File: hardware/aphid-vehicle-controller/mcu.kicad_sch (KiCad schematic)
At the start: 19 parts, among them J3 MAIN_DEBUG, J4 SWD, U1 STM32G491CETx, Y1 8 MHz

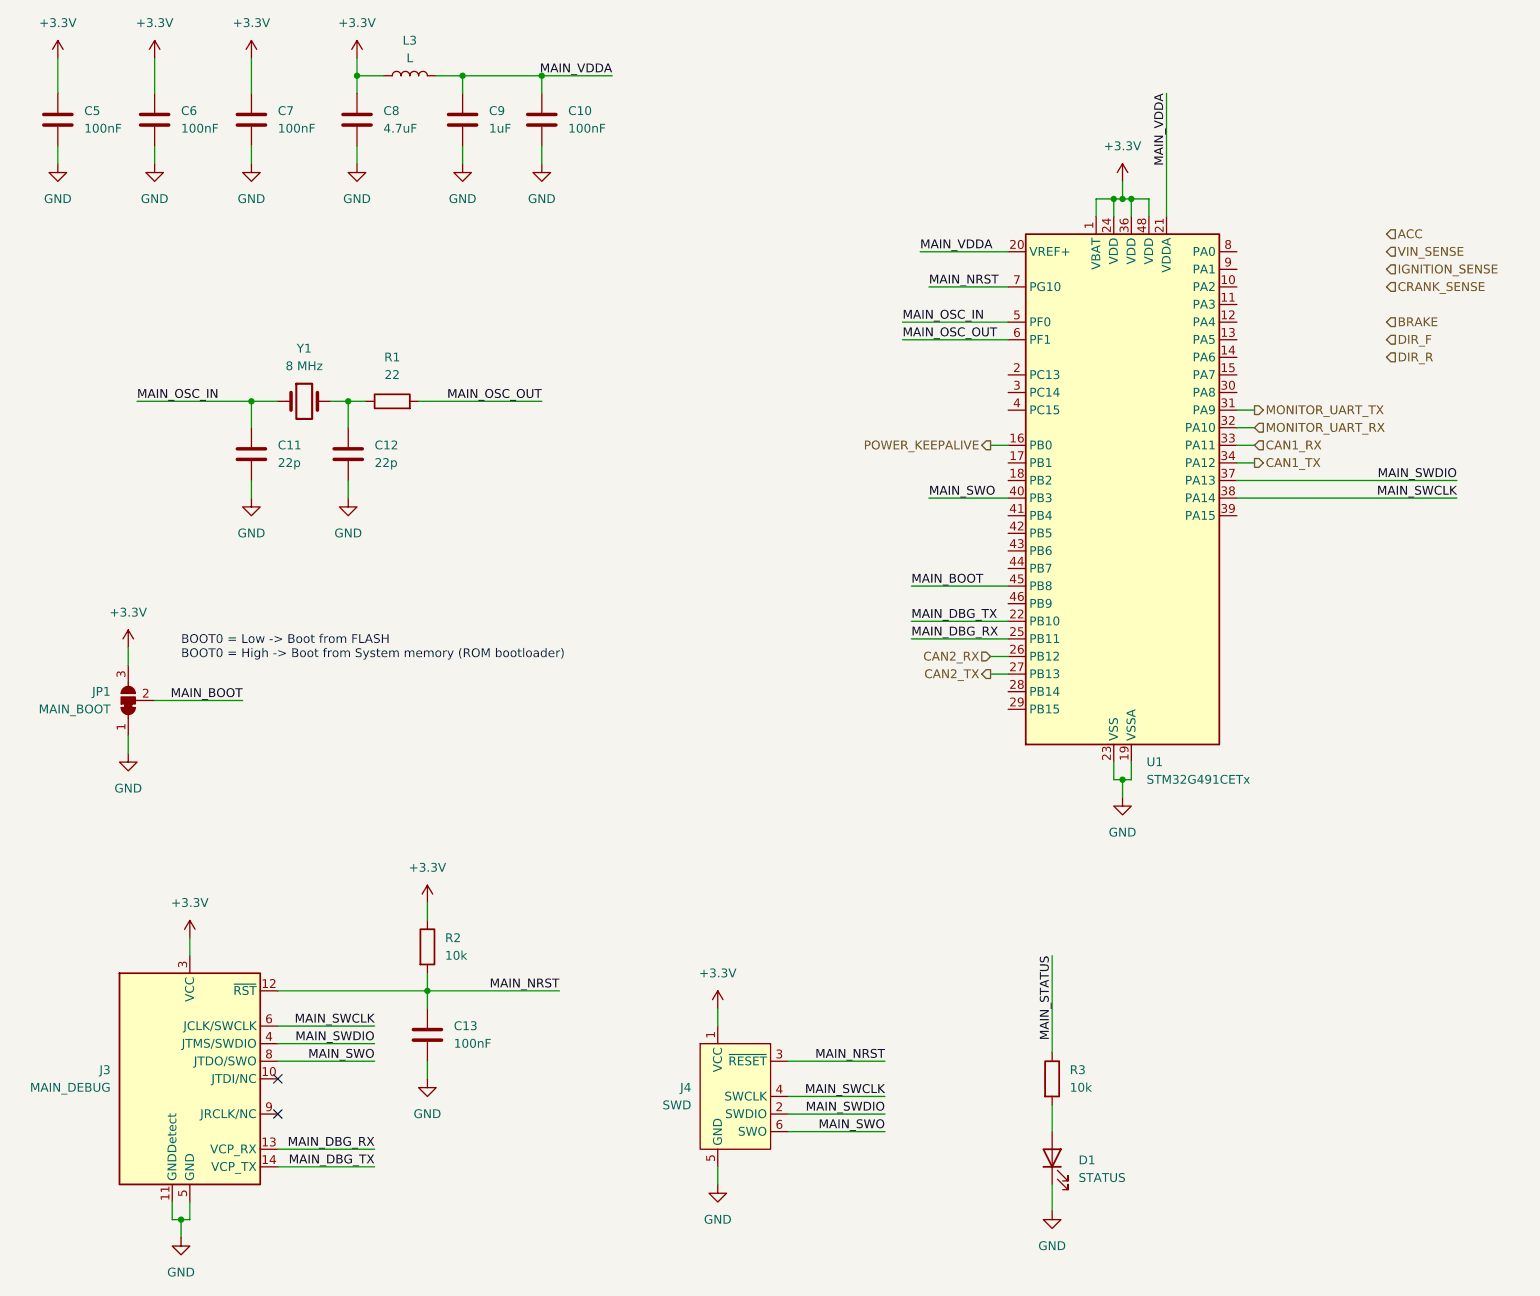
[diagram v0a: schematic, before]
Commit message: ERC check passing
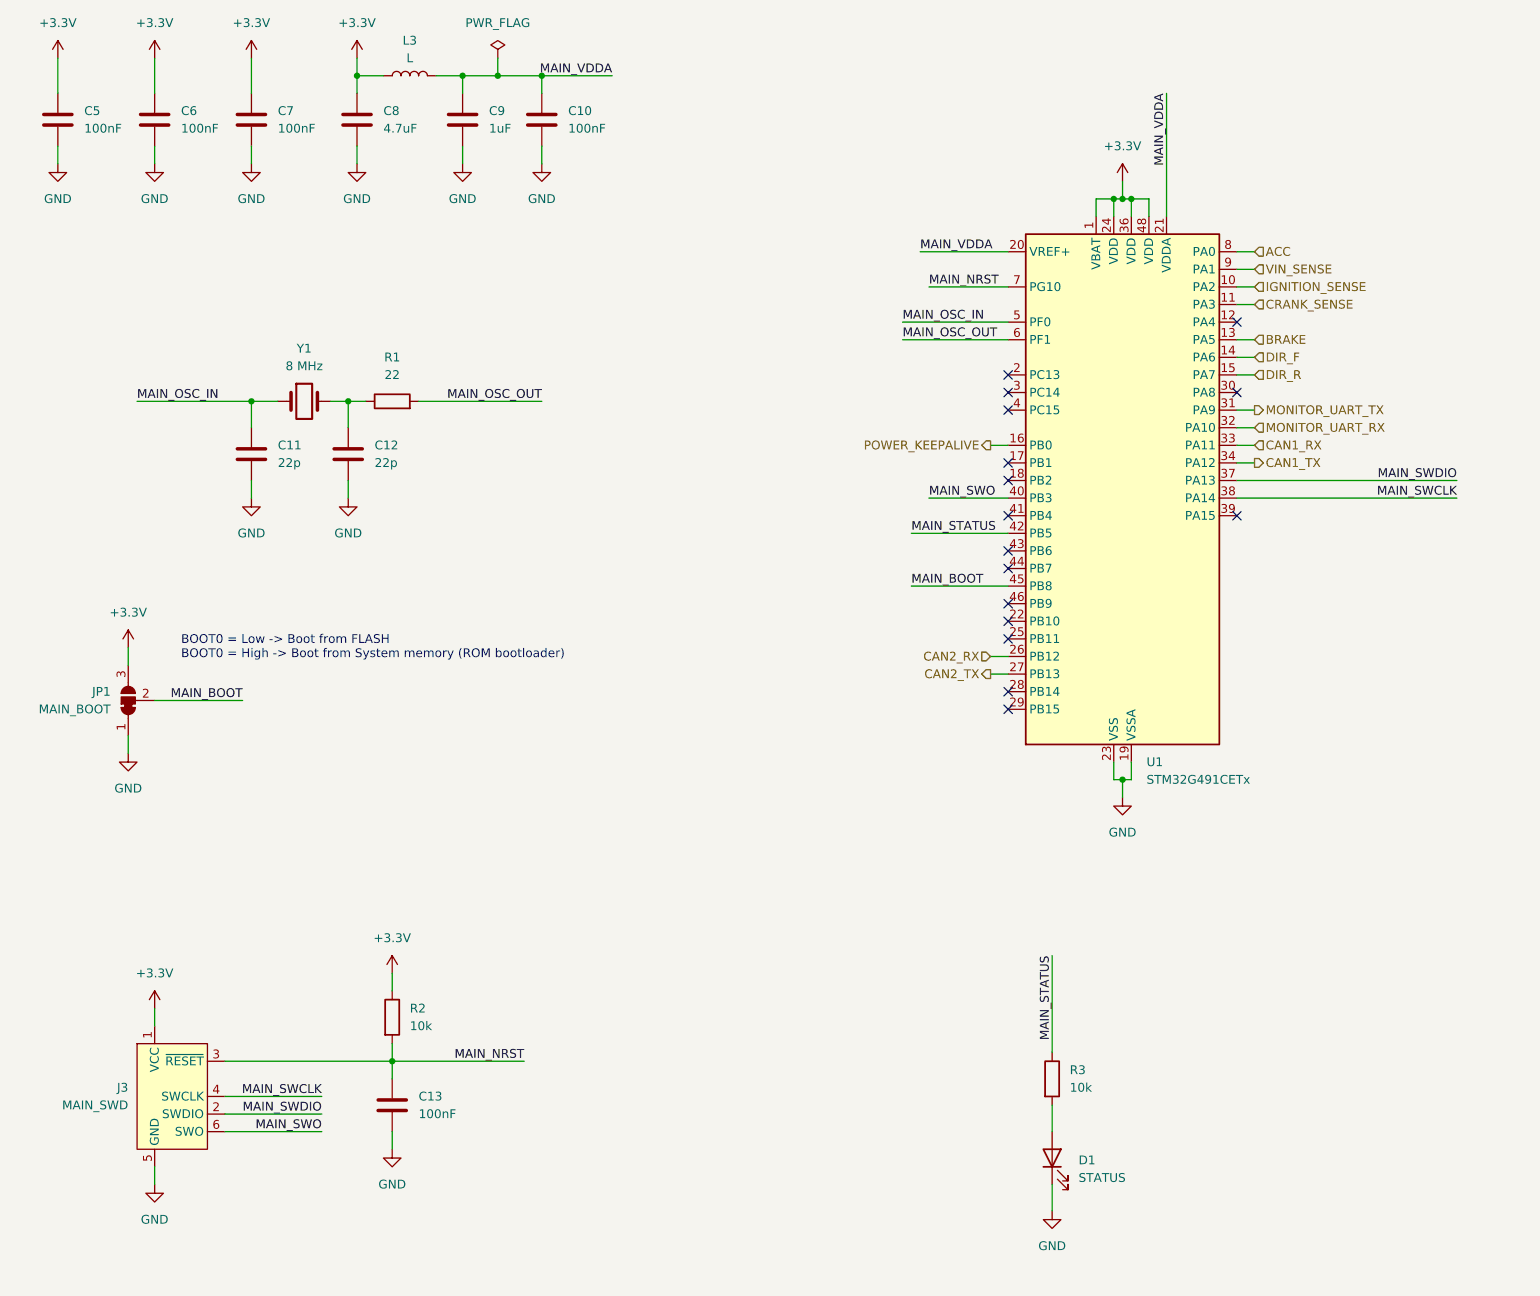
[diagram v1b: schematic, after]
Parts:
- removed J3: MAIN_DEBUG, Connector_PinHeader_1.27mm:PinHeader_2x07_P1.27mm_Vertical_SMD, symbol Connector:Conn_ST_STDC14
- J3: renamed from J4; value SWD -> MAIN_SWD
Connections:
- net ACC: now also U1.8 (PA0)
- net BRAKE: now also U1.13 (PA5)
- net CRANK_SENSE: now also U1.11 (PA3)
- net DIR_F: now also U1.14 (PA6)
- net DIR_R: now also U1.15 (PA7)
- net IGNITION_SENSE: now also U1.10 (PA2)
- net MAIN_STATUS: now also U1.42 (PB5)
- net VIN_SENSE: now also U1.9 (PA1)
- net MAIN_DBG_RX: no longer names the net of U1.25 (PB11)
- net MAIN_DBG_TX: no longer names the net of U1.22 (PB10)
- no-connect marks 2 -> 16
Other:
- moved on the sheet: C13, J3, R2

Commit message: Some cleaning up
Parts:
- JP1: footprint (none) -> Jumper:SolderJumper-3_P1.3mm_Bridged12_RoundedPad1.0x1.5mm
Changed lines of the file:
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@@
 			)
 		)
-		(property "Footprint" ""
+		(property "Footprint" "Jumper:SolderJumper-3_P1.3mm_Bridged12_RoundedPad1.0x1.5mm"
 			(at 27.94 113.03 0)
 			(effects
